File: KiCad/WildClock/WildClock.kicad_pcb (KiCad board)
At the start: 2 copper layers, 68 x 67 mm, 39 parts, among them J1 UART, Q1 CA1, Q2 CA2, Q3 CA3, Q4 CA4, Q5 CAL, SW1 ButtonUp, SW2 ButtonDown, SW3 ButtonOK, U1 ESP32-C3-MINI-1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

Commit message: make all clearer and neu pcb
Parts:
- removed REF** (x4): MountingHole_4.3mm_M4, MountingHole:MountingHole_4.3mm_M4
- BT1: moved to F.Cu
- R1, R15, R2, R3, R4, R5: value 1kOhm -> 1k
- R10, R11, R12, R13, R14, R7, R8, R9: value 150Ohm -> 150
- R16, R6: value 10kOhm -> 10k
- U2: value LTC-4627JR -> 7Segment
- moved BZ1 33.8 mm to (51.0, 56.2), turned to -90 degrees
- moved U2 31.2 mm to (61.0, 20.0), turned to -90 degrees
- moved BT1 26.4 mm to (102.0, 20.0), turned to -90 degrees
- moved SW3 25.0 mm to (25.8, 59.8)
- moved C3 24.9 mm to (37.0, 48.4)
- moved R7 22.2 mm to (70.0, 39.0), turned to 180 degrees
- moved S1 22.1 mm to (48.0, 50.0)
- moved R9 20.5 mm to (70.0, 41.0), turned to 180 degrees
- moved C2 19.5 mm to (28.0, 52.9)
- moved C1 19.1 mm to (26.0, 52.9)
- moved U3 19.1 mm to (62.0, 42.0)
- moved R11 18.9 mm to (70.0, 43.0), turned to 180 degrees
- moved R12 18.9 mm to (70.0, 45.0), turned to 180 degrees
- moved R15 17.6 mm to (30.0, 51.0), turned to -90 degrees
- moved R10 17.2 mm to (67.0, 41.0), turned to -90 degrees
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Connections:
- net Net-(BZ1-Pad1) renamed BUZZ
- net Net-(J1-Pad2) renamed TXD0
- net Net-(J1-Pad3) renamed RXD0
- net Net-(Q1-Pad3) renamed CA1
- net Net-(Q2-Pad3) renamed CA2
- net Net-(Q3-Pad3) renamed CA3
- net Net-(Q4-Pad3) renamed CA4
- net Net-(Q5-Pad3) renamed CAL
- net Net-(R1-Pad1) renamed Q1
- net Net-(R16-Pad1) renamed SWOK
- net Net-(R2-Pad1) renamed Q2
- net Net-(S1-Pad2) renamed TILT
- net Net-(SW1-Pad1) renamed SWUP
- net Net-(SW2-Pad1) renamed SWDOWN
- net Net-(U3-Pad11) renamed SRCLK
- BT1 pad 1: Net-(C1-Pad2) -> +3.3V
- BT1 pad 2: Net-(BT1-Pad2) -> GND
- C1 pad 1: Net-(BT1-Pad2) -> GND
- C1 pad 2: Net-(C1-Pad2) -> +3.3V
- C2 pad 1: Net-(BT1-Pad2) -> GND
- C2 pad 2: Net-(C1-Pad2) -> +3.3V
- C3 pad 1: Net-(C3-Pad1) -> GND
- C3 pad 2: Net-(BT1-Pad2) -> Net-(C3-Pad2)
- JP1 pad 2: Net-(JP1-Pad2) -> SER
- R10 pad 2: Net-(R10-Pad2) -> D
- R11 pad 2: Net-(R11-Pad2) -> E
- R12 pad 2: Net-(R12-Pad2) -> F
- R13 pad 2: Net-(R13-Pad2) -> G
- R14 pad 2: Net-(R14-Pad2) -> DP
- R15 pad 1: Net-(C1-Pad2) -> Net-(C3-Pad2)
- R15 pad 2: Net-(C3-Pad1) -> +3.3V
- R3 pad 1: Net-(R3-Pad1) -> Q3
- R4 pad 1: Net-(R4-Pad1) -> Q4
- R5 pad 1: Net-(R5-Pad1) -> QL
- R6 pad 1: Net-(R5-Pad1) -> Q4
- R7 pad 2: Net-(R7-Pad2) -> A
- R8 pad 2: Net-(R8-Pad2) -> B
- R9 pad 2: Net-(R9-Pad2) -> C
- U1 pad 1: Net-(BT1-Pad2) -> GND
- U1 pad 2: Net-(BT1-Pad2) -> GND
- U1 pad 20: Net-(R3-Pad1) -> QL
- U1 pad 21: Net-(R4-Pad1) -> Q3
- U1 pad 22: Net-(R5-Pad1) -> Q4
- U1 pad 23: Net-(U3-Pad14) -> SER
- U1 pad 26: Net-(JP1-Pad2) -> RCLK
- U1 pad 3: Net-(C1-Pad2) -> +3.3V
- U1 pad 36: Net-(BT1-Pad2) -> GND
- U1 pad 37: Net-(BT1-Pad2) -> GND
- U1 pad 38: Net-(BT1-Pad2) -> GND
- U1 pad 39: Net-(BT1-Pad2) -> GND
- U1 pad 40: Net-(BT1-Pad2) -> GND
- U1 pad 41: Net-(BT1-Pad2) -> GND
- U1 pad 42: Net-(BT1-Pad2) -> GND
- U1 pad 43: Net-(BT1-Pad2) -> GND
- U1 pad 44: Net-(BT1-Pad2) -> GND
- U1 pad 45: Net-(BT1-Pad2) -> GND
- U1 pad 46: Net-(BT1-Pad2) -> GND
- U1 pad 47: Net-(BT1-Pad2) -> GND
- U1 pad 48: Net-(BT1-Pad2) -> GND
- U1 pad 49: Net-(BT1-Pad2) -> GND
- U1 pad 50: Net-(BT1-Pad2) -> GND
- U1 pad 51: Net-(BT1-Pad2) -> GND
- U1 pad 52: Net-(BT1-Pad2) -> GND
- U1 pad 53: Net-(BT1-Pad2) -> GND
- U1 pad 8: Net-(C3-Pad1) -> Net-(C3-Pad2)
- U2 pad 11: Net-(R9-Pad2) -> Net-(R12-Pad1)
- U2 pad 13: Net-(R12-Pad2) -> Net-(R9-Pad1)
- U2 pad 14: Net-(R14-Pad2) -> Net-(R7-Pad1)
- U2 pad 15: Net-(R8-Pad2) -> Net-(R13-Pad1)
- U2 pad 16: Net-(R13-Pad2) -> Net-(R8-Pad1)
- U2 pad 3: Net-(R11-Pad2) -> Net-(R10-Pad1)
- U2 pad 5: Net-(R10-Pad2) -> Net-(R11-Pad1)
- U2 pad 7: Net-(R7-Pad2) -> Net-(R14-Pad1)
- U3 pad 1: Net-(R13-Pad1) -> G
- U3 pad 12: Net-(JP1-Pad2) -> RCLK
- U3 pad 14: Net-(U3-Pad14) -> SER
- U3 pad 15: Net-(R14-Pad1) -> DP
- U3 pad 2: Net-(R12-Pad1) -> F
- U3 pad 3: Net-(R11-Pad1) -> E
- U3 pad 4: Net-(R10-Pad1) -> D
- U3 pad 5: Net-(R9-Pad1) -> C
- U3 pad 6: Net-(R8-Pad1) -> B
- U3 pad 7: Net-(R7-Pad1) -> A
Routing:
- net Net-(BT1-Pad2): track 156.7 -> 0.00 mm, vias 3 -> 0
- net Net-(C1-Pad2): track 103.6 -> 0.00 mm, vias 1 -> 0
- net Net-(R7-Pad2): track 82.5 -> 0.00 mm
- net Net-(R11-Pad2): track 60.8 -> 0.00 mm
- net Net-(C3-Pad1): track 58.5 -> 0.00 mm
- net Net-(R14-Pad1): track 18.5 -> 75.9 mm
- net SER: track 0.00 -> 50.3 mm, vias 0 -> 2
- net Net-(R8-Pad2): track 45.0 -> 0.00 mm
- net TILT: track 5.32 -> 50.3 mm, vias 0 -> 1
- net Net-(R11-Pad1): track 3.65 -> 45.5 mm
- net RCLK: track 0.00 -> 41.2 mm, vias 0 -> 2
- net CAL: track 61.5 -> 23.0 mm
- net Net-(JP1-Pad2): track 33.4 -> 0.00 mm
- net Net-(U3-Pad14): track 29.6 -> 0.00 mm
- net Net-(R12-Pad1): track 3.95 -> 32.9 mm, vias 0 -> 1
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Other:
- board outline removed

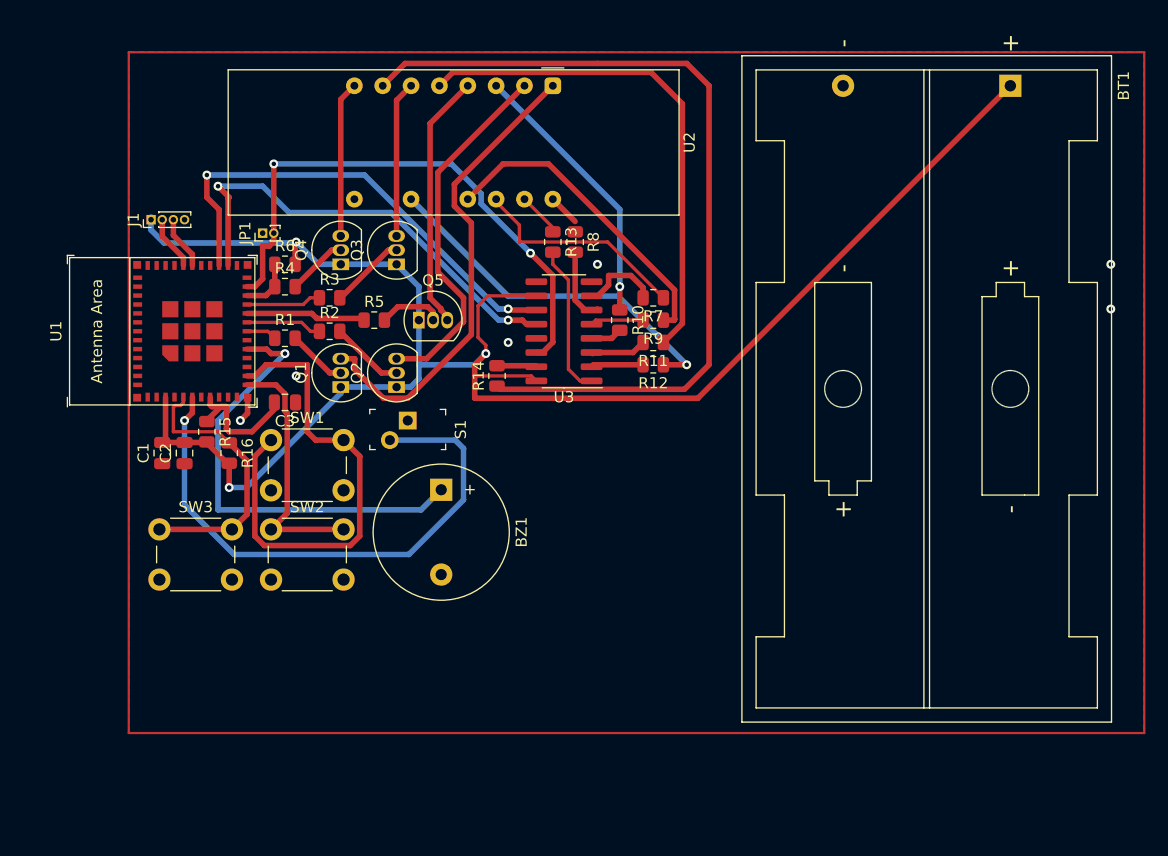
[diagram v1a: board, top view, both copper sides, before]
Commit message: changed some footprints
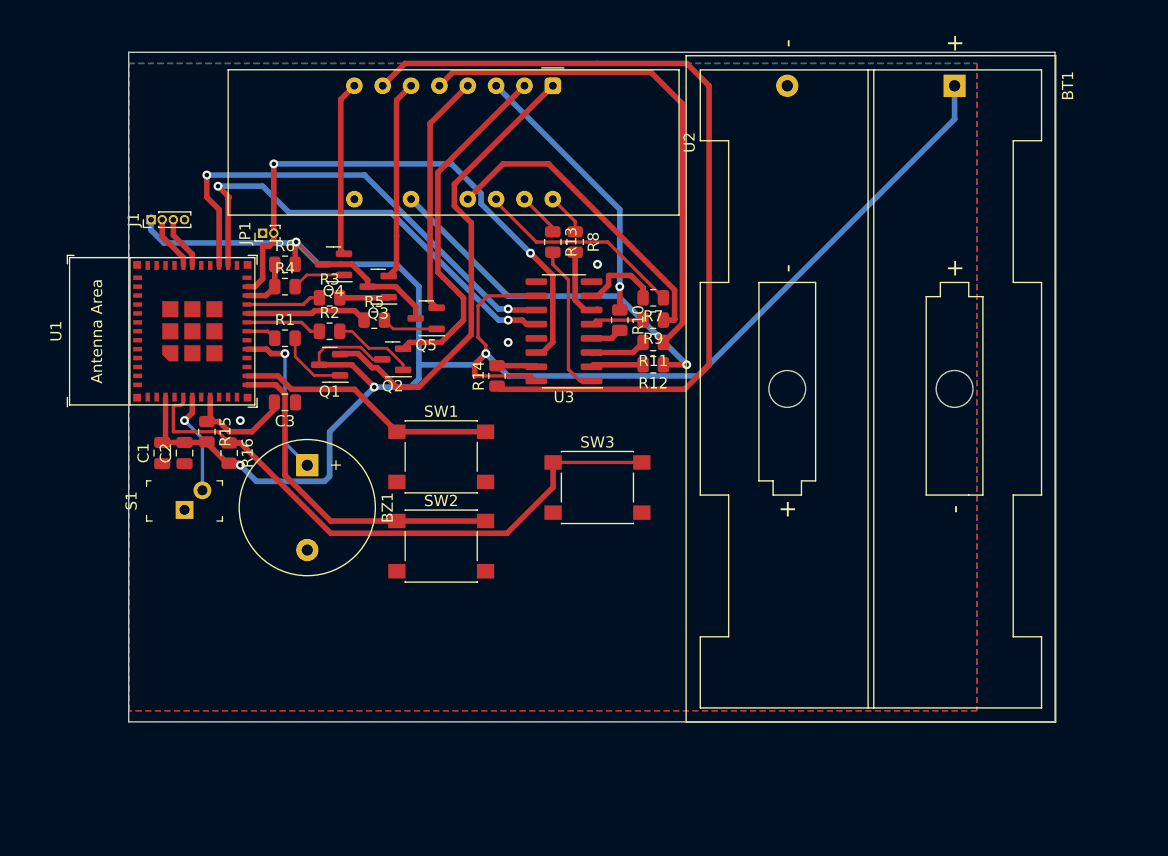
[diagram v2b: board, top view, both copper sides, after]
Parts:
- Q1, Q2, Q3, Q4, Q5: footprint Package_TO_SOT_THT:TO-92_Inline -> Package_TO_SOT_SMD:SOT-23
- SW1, SW2, SW3: footprint Button_Switch_THT:SW_PUSH_6mm -> Button_Switch_SMD:SW_Push_1P1T_NO_6x6mm_H9.5mm
- moved SW3 39.4 mm to (65.0, 56.0)
- moved S1 21.5 mm to (28.0, 58.0), turned to 90 degrees
- moved SW1 15.3 mm to (51.0, 53.2)
- moved SW2 15.3 mm to (51.0, 61.2)
- moved BZ1 12.2 mm to (39.0, 54.0)
- moved BT1 5.00 mm to (97.0, 20.0)
- moved Q3 2.59 mm to (45.4, 38.0), turned to 180 degrees
- moved Q2 2.51 mm to (46.6, 44.5), turned to 180 degrees
- moved Q1 2.24 mm to (41.0, 45.0), turned to 180 degrees
- moved Q5 0.67 mm to (49.6, 40.8), turned to 180 degrees
- moved Q4 0.65 mm to (41.4, 36.0), turned to 180 degrees
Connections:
- Q1 pad 1: +3.3V -> Net-(R1-Pad2)
- Q1 pad 2: Net-(Q1-Pad2) -> CA1
- Q1 pad 3: CA1 -> +3.3V
- Q2 pad 1: +3.3V -> Net-(R2-Pad2)
- Q2 pad 2: Net-(Q2-Pad2) -> CA2
- Q2 pad 3: CA2 -> +3.3V
- Q3 pad 1: +3.3V -> Net-(R3-Pad2)
- Q3 pad 2: Net-(Q3-Pad2) -> CA3
- Q3 pad 3: CA3 -> +3.3V
- Q4 pad 1: +3.3V -> Net-(R4-Pad2)
- Q4 pad 2: Net-(R4-Pad2) -> CA4
- Q4 pad 3: CA4 -> +3.3V
- Q5 pad 1: +3.3V -> Net-(R5-Pad2)
- Q5 pad 2: Net-(Q5-Pad2) -> CAL
- Q5 pad 3: CAL -> +3.3V
- R1 pad 2: Net-(Q1-Pad2) -> Net-(R1-Pad2)
- R2 pad 2: Net-(Q2-Pad2) -> Net-(R2-Pad2)
- R3 pad 2: Net-(Q3-Pad2) -> Net-(R3-Pad2)
- R5 pad 2: Net-(Q5-Pad2) -> Net-(R5-Pad2)
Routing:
- net TILT: track 50.3 -> 9.30 mm
- net SWOK: track 24.7 -> 53.5 mm
- net BUZZ: track 40.8 -> 14.6 mm
- net +3.3V: track 158.5 -> 180.1 mm, vias 3 -> 4
- net SWUP: track 43.9 -> 23.4 mm
- net SWDOWN: track 23.1 -> 30.7 mm
- net Net-(R2-Pad2): track 0.00 -> 7.40 mm
- net Net-(Q3-Pad2): track 6.86 -> 0.00 mm
- net Net-(Q2-Pad2): track 6.63 -> 0.00 mm
- net Net-(R1-Pad2): track 0.00 -> 6.36 mm
- net Net-(Q5-Pad2): track 5.78 -> 0.00 mm
- net Net-(Q1-Pad2): track 5.37 -> 0.00 mm
- net Net-(R5-Pad2): track 0.00 -> 5.00 mm
- net Net-(R3-Pad2): track 0.00 -> 4.40 mm
- net CA3: track 14.3 -> 17.9 mm
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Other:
- board outline added: 83 x 60 mm

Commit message: start updating footprints to match jlcpcb
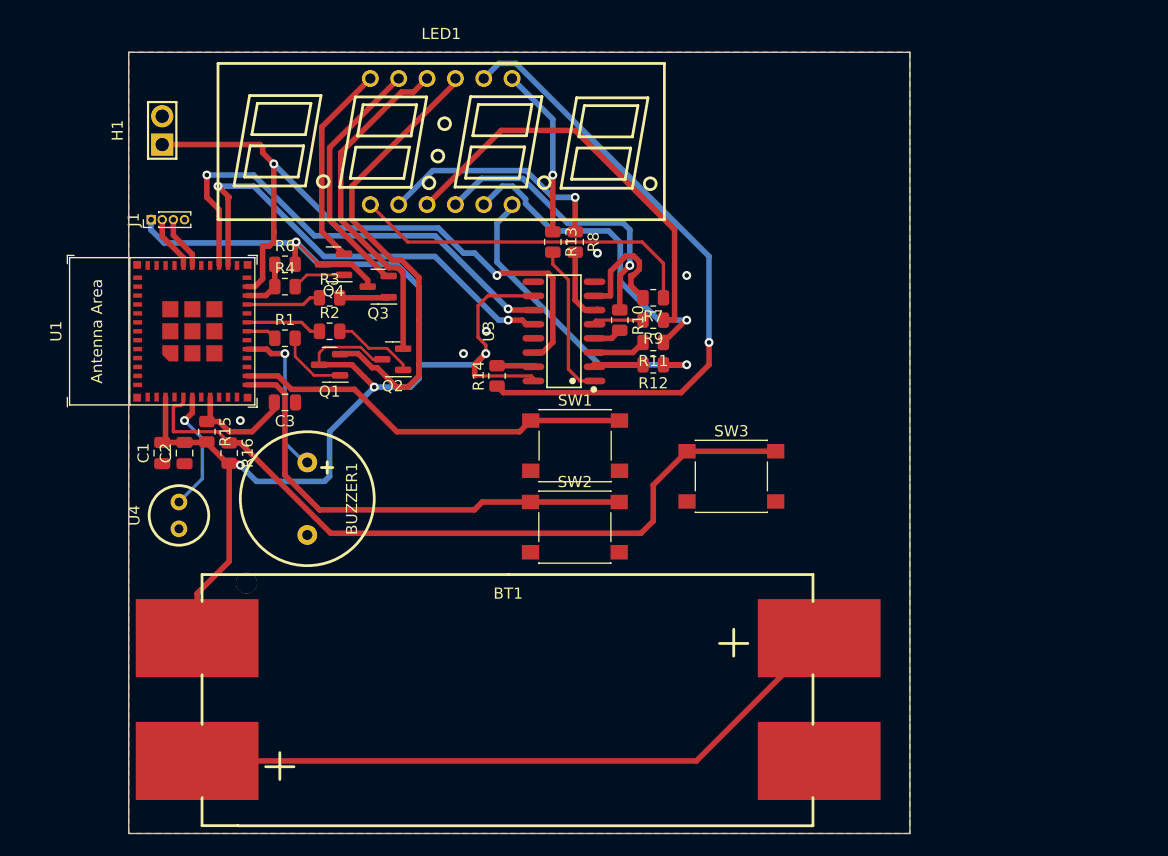
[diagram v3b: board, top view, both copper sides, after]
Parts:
- removed BZ1: Buzzer, Buzzer_Beeper:Buzzer_12x9.5RM7.6
- removed JP1: Jumper_BOOT, Connector_PinHeader_1.00mm:PinHeader_1x02_P1.00mm_Vertical
- removed Q5: CAL, Package_TO_SOT_SMD:SOT-23
- removed R5: 1k, Resistor_SMD:R_0805_2012Metric
- removed S1: tilt sensor, digikey-footprints:Tilt_Switch_RB-220-07A_R
- removed U2: 7Segment, Display_7Segment:LTC-4627Jx
- added BUZZER1: GMC1209YB-25R2048, easyeda2kicad:BUZ-TH_BD12.0-P6.50-D0.6-FD, F.Cu at (39.0, 57.0)
- added H1: PZ254-1-02-Z-8.5, easyeda2kicad:HDR-TH_2P-P2.54-V-M, F.Cu at (26.0, 24.0)
- added LED1: SLR0394DBA5BD, easyeda2kicad:LED-SEG-TH_SLR0394DBA5BD, F.Cu at (51.0, 25.0)
- added U4: TiltSensor, easyeda2kicad:SENSOR-TH_SW-520DS-AB12G, F.Cu at (27.5, 58.5)
- BT1: value Battery -> aaa bp; footprint Battery:BatteryHolder_Keystone_2462_2xAA -> easyeda2kicad:BAT-SMD_BH-AAA-B5AA001
- U3: footprint Package_SO:SOIC-16_3.9x9.9mm_P1.27mm -> easyeda2kicad:SOIC-16_L9.9-W3.9-P1.27-LS6.0-BL
- moved BT1 68.0 mm to (57.0, 75.0), turned to 0 degrees
- moved SW2 12.1 mm to (63.0, 59.5)
- moved SW1 12.0 mm to (63.0, 52.2)
- moved SW3 12.0 mm to (77.0, 55.0)
- turned U3 to 90 degrees
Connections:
- BT1 pad 1: +3.3V -> Net-(BT1-Pad1)
- BT1 pad 2: GND -> +3.3V
- Q1 pad 2: CA1 -> CA4
- Q2 pad 2: CA2 -> CA3
- Q3 pad 2: CA3 -> CA2
- Q4 pad 2: CA4 -> CA1
- U1 pad 20: QL -> unconnected-(U1-Pad20)
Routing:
- net Net-(BT1-Pad1): track 0.00 -> 60.3 mm
- net +3.3V: track 180.1 -> 135.6 mm
- net CA4: track 15.7 -> 42.2 mm
- net CA1: track 41.6 -> 18.7 mm
- net CAL: track 21.5 -> 0.00 mm
- net Net-(LED1-Pad8): track 75.9 -> 57.9 mm, vias 0 -> 1
- net Net-(R8-Pad1): track 3.76 -> 21.2 mm, vias 0 -> 1
- net Net-(R11-Pad1): track 45.5 -> 28.5 mm, vias 0 -> 1
- net CA3: track 17.9 -> 31.4 mm
- net SWOK: track 53.5 -> 66.5 mm
- net Net-(R7-Pad1): track 18.8 -> 31.5 mm
- net SWUP: track 23.4 -> 35.9 mm
- net SWDOWN: track 30.7 -> 42.5 mm
- net Net-(R13-Pad1): track 3.59 -> 15.2 mm, vias 0 -> 1
- net QL: track 10.9 -> 0.00 mm
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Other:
- board size 83 x 60 mm -> 70 x 70 mm

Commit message: use lcsc footprints
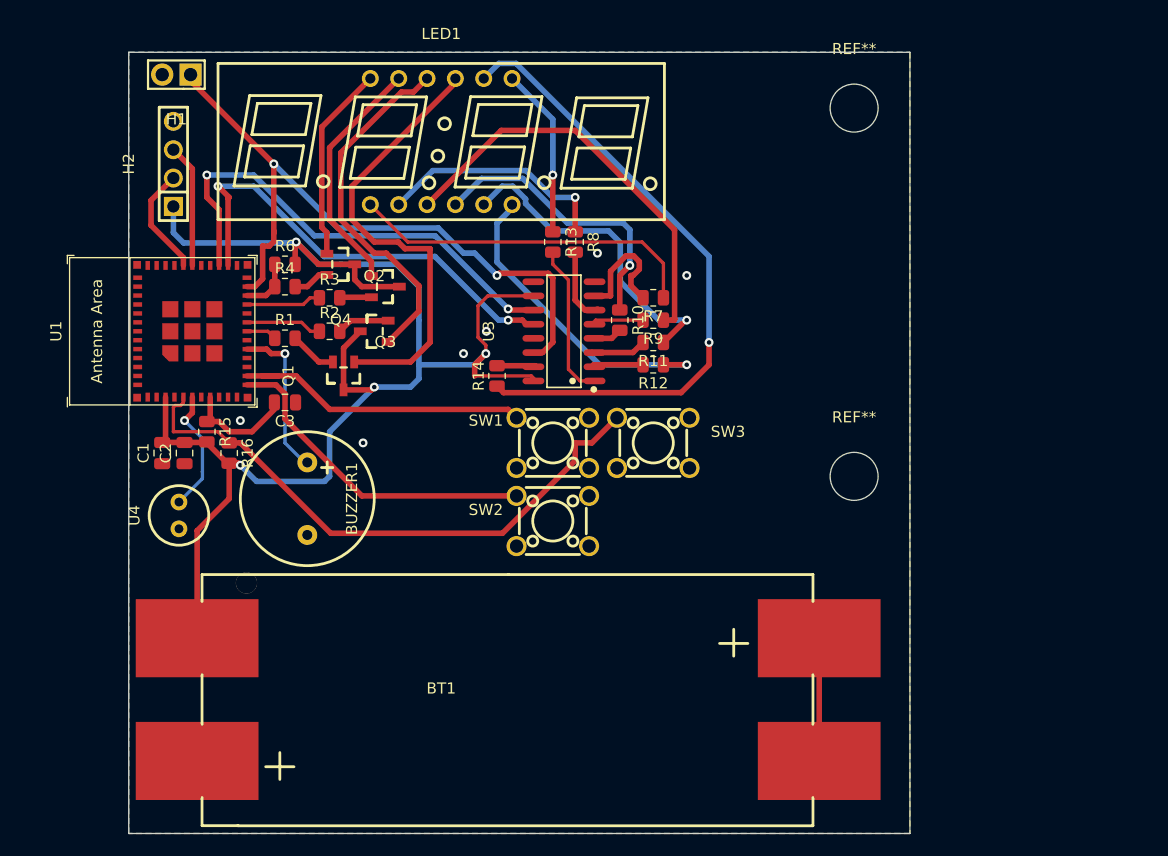
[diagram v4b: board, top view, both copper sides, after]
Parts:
- removed J1: UART, Connector_PinHeader_1.00mm:PinHeader_1x04_P1.00mm_Vertical
- added H2: UART, easyeda2kicad:HDR-TH_4P-P2.54-V-M, F.Cu at (27.0, 27.0)
- added REF**: MountingHole_4.3mm_M4, MountingHole:MountingHole_4.3mm_M4, F.Cu at (88.0, 22.0)
- added REF**: MountingHole_4.3mm_M4, MountingHole:MountingHole_4.3mm_M4, F.Cu at (88.0, 55.0)
- Q1, Q2, Q3, Q4: footprint Package_TO_SOT_SMD:SOT-23 -> easyeda2kicad:SOT-23-3_L2.9-W1.3-P1.90-LS2.4-BR-CW
- SW1: value ButtonUp -> SWUP; footprint Button_Switch_SMD:SW_Push_1P1T_NO_6x6mm_H9.5mm -> easyeda2kicad:SW-TH_4P-L6.0-W6.0-P4.50-LS6.5
- SW2: value ButtonDown -> SWDOWN; footprint Button_Switch_SMD:SW_Push_1P1T_NO_6x6mm_H9.5mm -> easyeda2kicad:SW-TH_4P-L6.0-W6.0-P4.50-LS6.5
- SW3: value ButtonOK -> SWOK; footprint Button_Switch_SMD:SW_Push_1P1T_NO_6x6mm_H9.5mm -> easyeda2kicad:SW-TH_4P-L6.0-W6.0-P4.50-LS6.5
- moved SW3 7.62 mm to (70.0, 52.0)
- moved H1 5.16 mm to (27.3, 19.0), turned to 180 degrees
- moved Q2 3.01 mm to (45.0, 42.0), turned to 0 degrees
- moved SW2 2.05 mm to (61.0, 59.0)
- moved SW1 2.02 mm to (61.0, 52.0)
- moved Q1 1.60 mm to (42.2, 46.0), turned to 90 degrees
- moved Q3 0.65 mm to (46.0, 38.0)
- moved Q4 0.65 mm to (42.0, 36.0)
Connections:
- BT1 pad 3: Net-(BT1-Pad1) -> GND
- BT1 pad 4: GND -> Net-(BT1-Pad1)
- Q1 pad 1: Net-(Q1-Pad1) -> CA4
- Q1 pad 2: CA4 -> +3.3V
- Q1 pad 3: +3.3V -> Net-(Q1-Pad3)
- Q2 pad 1: Net-(Q2-Pad1) -> CA3
- Q2 pad 2: CA3 -> +3.3V
- Q2 pad 3: +3.3V -> Net-(Q2-Pad3)
- Q3 pad 1: Net-(Q3-Pad1) -> CA2
- Q3 pad 2: CA2 -> +3.3V
- Q3 pad 3: +3.3V -> Net-(Q3-Pad3)
- Q4 pad 1: Net-(Q4-Pad1) -> CA1
- Q4 pad 2: CA1 -> +3.3V
- Q4 pad 3: +3.3V -> Net-(Q4-Pad3)
- R1 pad 2: Net-(Q1-Pad1) -> Net-(Q1-Pad3)
- R2 pad 2: Net-(Q2-Pad1) -> Net-(Q2-Pad3)
- R3 pad 2: Net-(Q3-Pad1) -> Net-(Q3-Pad3)
- R4 pad 2: Net-(Q4-Pad1) -> Net-(Q4-Pad3)
- SW1 pad 2: GND -> unconnected-(SW1-Pad2)
- SW2 pad 2: GND -> unconnected-(SW2-Pad2)
- SW3 pad 2: GND -> unconnected-(SW3-Pad2)
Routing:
- net Net-(BT1-Pad1): track 60.3 -> 11.0 mm
- net SWOK: track 66.5 -> 52.6 mm
- net SWDOWN: track 42.5 -> 29.6 mm
- net SWUP: track 35.9 -> 27.1 mm
- net Net-(Q2-Pad1): track 7.40 -> 0.00 mm
- net Net-(Q1-Pad1): track 6.36 -> 0.00 mm
- net RXD0: track 4.80 -> 11.1 mm
- net TXD0: track 4.89 -> 9.86 mm
- net Net-(Q4-Pad1): track 4.81 -> 0.00 mm
- net Net-(Q2-Pad3): track 0.00 -> 4.73 mm
- net Net-(Q3-Pad1): track 4.40 -> 0.00 mm
- net Net-(Q1-Pad3): track 0.00 -> 4.27 mm
- net Net-(Q4-Pad3): track 0.00 -> 3.27 mm
- net Net-(Q3-Pad3): track 0.00 -> 2.86 mm
- net CA4: track 42.2 -> 40.5 mm
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
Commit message: implemented maxis changes
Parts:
- added Q5: AO3400A, Package_TO_SOT_SMD:SOT-23, F.Cu at (47.5, 57.5)
- added R5: 1k, Resistor_SMD:R_0805_2012Metric, F.Cu at (38.0, 38.5)
- Q1: value CA1 -> AO3401A; footprint easyeda2kicad:SOT-23-3_L2.9-W1.3-P1.90-LS2.4-BR-CW -> Package_TO_SOT_SMD:SOT-23
- Q2: value CA2 -> AO3401A; footprint easyeda2kicad:SOT-23-3_L2.9-W1.3-P1.90-LS2.4-BR-CW -> Package_TO_SOT_SMD:SOT-23
- Q3: value CA3 -> AO3401A; footprint easyeda2kicad:SOT-23-3_L2.9-W1.3-P1.90-LS2.4-BR-CW -> Package_TO_SOT_SMD:SOT-23
- Q4: value CA4 -> AO3401A; footprint easyeda2kicad:SOT-23-3_L2.9-W1.3-P1.90-LS2.4-BR-CW -> Package_TO_SOT_SMD:SOT-23
- R2: value 1k -> 70
- moved R2 21.7 mm to (31.5, 61.5)
- moved R3 4.61 mm to (38.0, 42.5), turned to 180 degrees
- moved Q3 4.42 mm to (42.1, 40.0), turned to 0 degrees
- moved Q2 3.30 mm to (42.1, 43.5)
- moved R4 2.69 mm to (38.0, 40.5), turned to 180 degrees
- moved R1 2.12 mm to (38.0, 44.5), turned to 180 degrees
- moved Q1 1.02 mm to (42.1, 47.0), turned to 0 degrees
- moved BUZZER1 1.00 mm to (38.0, 57.0), turned to 90 degrees
- moved R6 1.00 mm to (38.0, 36.0)
- moved Q4 0.50 mm to (42.1, 36.5), turned to 0 degrees
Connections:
- BUZZER1 pad 1: BUZZ -> Net-(BUZZER1-+)
- BUZZER1 pad 2: GND -> Net-(BUZZER1--)
- Q1 pad 1: CA4 -> Net-(Q1-G)
- Q1 pad 3: Net-(Q1-Pad3) -> CA4
- Q2 pad 1: CA3 -> Net-(Q2-G)
- Q2 pad 3: Net-(Q2-Pad3) -> CA3
- Q3 pad 1: CA2 -> Net-(Q3-G)
- Q3 pad 3: Net-(Q3-Pad3) -> CA2
- Q4 pad 1: CA1 -> Net-(Q4-G)
- Q4 pad 3: Net-(Q4-Pad3) -> CA1
- R1 pad 1: Q1 -> Net-(Q1-G)
- R1 pad 2: Net-(Q1-Pad3) -> Q1
- R2 pad 1: Q2 -> +3.3V
- R2 pad 2: Net-(Q2-Pad3) -> Net-(BUZZER1-+)
- R3 pad 1: Q3 -> Net-(Q2-G)
- R3 pad 2: Net-(Q3-Pad3) -> Q2
- R4 pad 1: Q4 -> Net-(Q3-G)
- R4 pad 2: Net-(Q4-Pad3) -> Q3
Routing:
- net +3.3V: track 134.2 -> 160.4 mm
- net BUZZ: track 14.6 -> 27.3 mm, vias 1 -> 2
- net Net-(BUZZER1--): track 0.00 -> 10.1 mm
- net CA4: track 40.5 -> 33.8 mm
- net Net-(BUZZER1-+): track 0.00 -> 6.11 mm
- net Net-(Q2-Pad3): track 4.73 -> 0.00 mm
- net Net-(Q1-Pad3): track 4.27 -> 0.00 mm
- net Net-(Q4-G): track 0.00 -> 3.87 mm
- net Net-(Q4-Pad3): track 3.27 -> 0.00 mm
- net CA2: track 21.8 -> 25.0 mm
- net Q1: track 2.75 -> 5.63 mm
- net Q3: track 6.74 -> 3.86 mm
- net Net-(Q3-Pad3): track 2.86 -> 0.00 mm
- net Net-(Q1-G): track 0.00 -> 2.85 mm
- net Net-(Q3-G): track 0.00 -> 2.81 mm
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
